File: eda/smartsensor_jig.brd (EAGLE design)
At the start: 33 x 27.9 mm, 12 parts, among them J2 AVR_SPI_PRG_6PTH

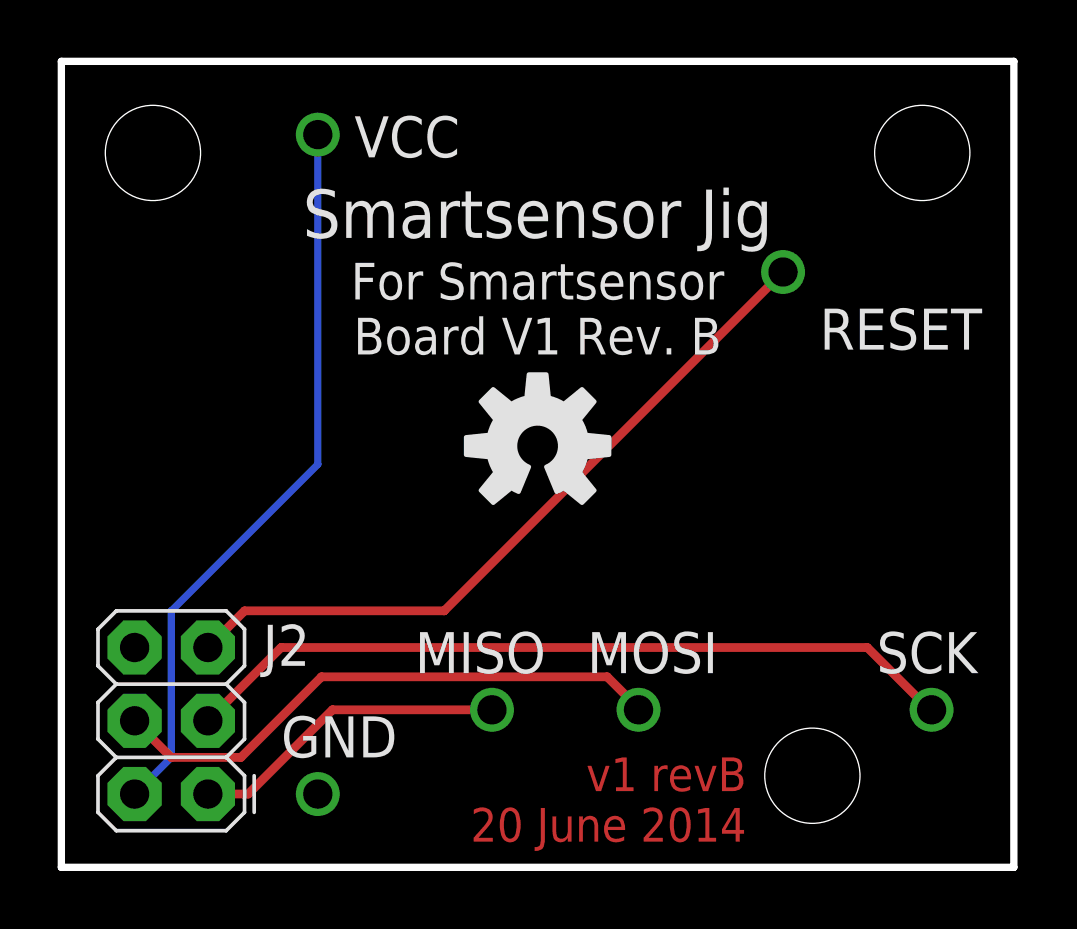
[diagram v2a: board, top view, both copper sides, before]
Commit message: All jigs probe vias accessible after populating.
Also changed "VCC" signal name on jigs to "5V" to match boards.
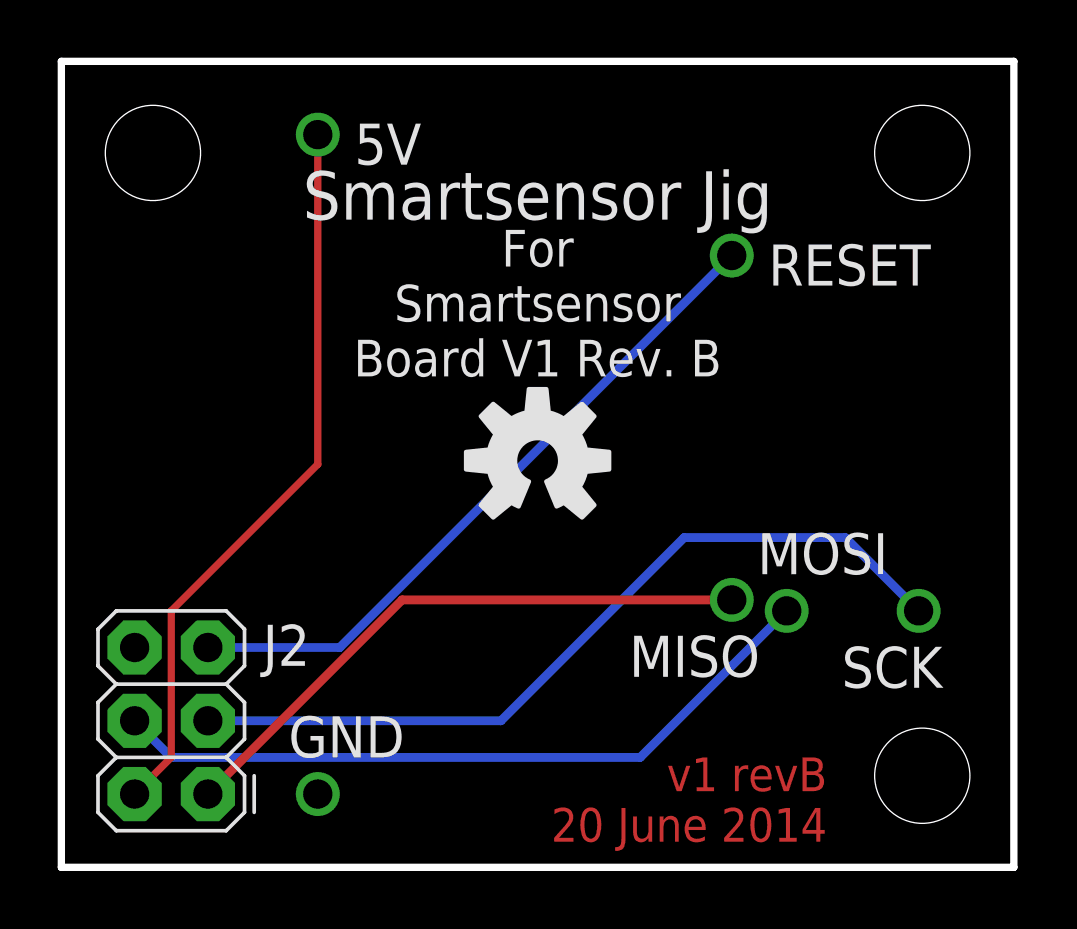
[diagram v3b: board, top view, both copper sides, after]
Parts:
- moved MISO 9.14 mm to (23.2, 9.27)
- moved MOSI 6.18 mm to (25.1, 8.89)
- moved U$3 3.81 mm to (29.8, 3.17)
- moved SCK 3.46 mm to (29.7, 8.89)
- moved RESET 1.87 mm to (23.2, 21.2)
- moved U$1 0.51 mm to (16.5, 14.1)
- renumbered VCC to 5V
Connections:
- net VCC renamed 5V
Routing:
- net MISO: track 11.1 -> 20.9 mm
- net MOSI: track 19.7 -> 25.2 mm
- net RESET: track 25.3 -> 23.8 mm
- net SCK: track 27.0 -> 28.3 mm

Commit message: Standardized copyright and "Design by" info among boards.
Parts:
- moved U$2 3.81 mm to (16.5, 6.99)
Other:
- board text added: "(c) Pioneers in Engineering. Design by: Krystyn Neisess. This design is open source hardware. For more information, visit pioneers.berkeley.edu/opensource."
- board text removed: "(c) Pioneers in Engineering Design by: Krystyn Neisess This design is open source hardware. For more information visit pioneers.berkeley.edu/opensource"
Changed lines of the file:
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@@
 <layer number="20" name="Dimension" color="15" fill="1" visible="yes" active="yes"/>
 <layer number="21" name="tPlace" color="16" fill="1" visible="yes" active="yes"/>
-<layer number="22" name="bPlace" color="17" fill="1" visible="no" active="yes"/>
+<layer number="22" name="bPlace" color="17" fill="1" visible="yes" active="yes"/>
 <layer number="23" name="tOrigins" color="15" fill="1" visible="yes" active="yes"/>
 <layer number="24" name="bOrigins" color="15" fill="1" visible="yes" active="yes"/>
@@
 <wire x1="33.02" y1="27.94" x2="0" y2="27.94" width="0.254" layer="20"/>
 <wire x1="0" y1="27.94" x2="0" y2="0" width="0.254" layer="20"/>
-<text x="22.86" y="23.495" size="0.762" layer="22" font="vector" ratio="20" rot="SMR0" align="top-left">(c) Pioneers in Engineering
-Design by:
-Krystyn Neisess
-This design is
-open source hardware.
-For more information visit
-pioneers.berkeley.edu/opensource</text>
+<text x="16.51" y="19.685" size="0.889" layer="22" font="vector" ratio="15" rot="SMR0" align="top-center">(c) Pioneers in Engineering.
+Design by:  Krystyn Neisess.
+This design is open source hardware.
+For more information, visit
+pioneers.berkeley.edu/opensource.</text>
 <text x="16.51" y="24.13" size="1.6764" layer="21" font="vector" ratio="15" align="top-center">Smartsensor Jig</text>
 <text x="16.51" y="22.098" size="1.27" layer="21" font="vector" ratio="15" align="top-center">For
@@
 </element>
 <element name="U$1" library="pie" package="OSHW-LOGO-M" value="" x="16.51" y="14.097"/>
-<element name="U$2" library="pie" package="PIE-LOGO-SMALL" value="" x="16.51" y="10.795" rot="MR0"/>
+<element name="U$2" library="pie" package="PIE-LOGO-SMALL" value="" x="16.51" y="6.985" rot="MR0"/>
 <element name="U$3" library="pie" package="STAND-OFF" value="" x="29.845" y="3.175"/>
 <element name="U$4" library="pie" package="STAND-OFF" value="" x="3.175" y="24.765"/>
